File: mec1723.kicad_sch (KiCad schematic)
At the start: 19 parts, among them SW3001 SW_B3U-1000P_SMD, U3001 MEC1723N-B0-I/SZ, Y3001 Resonator_32.768kHz_ECX-31B

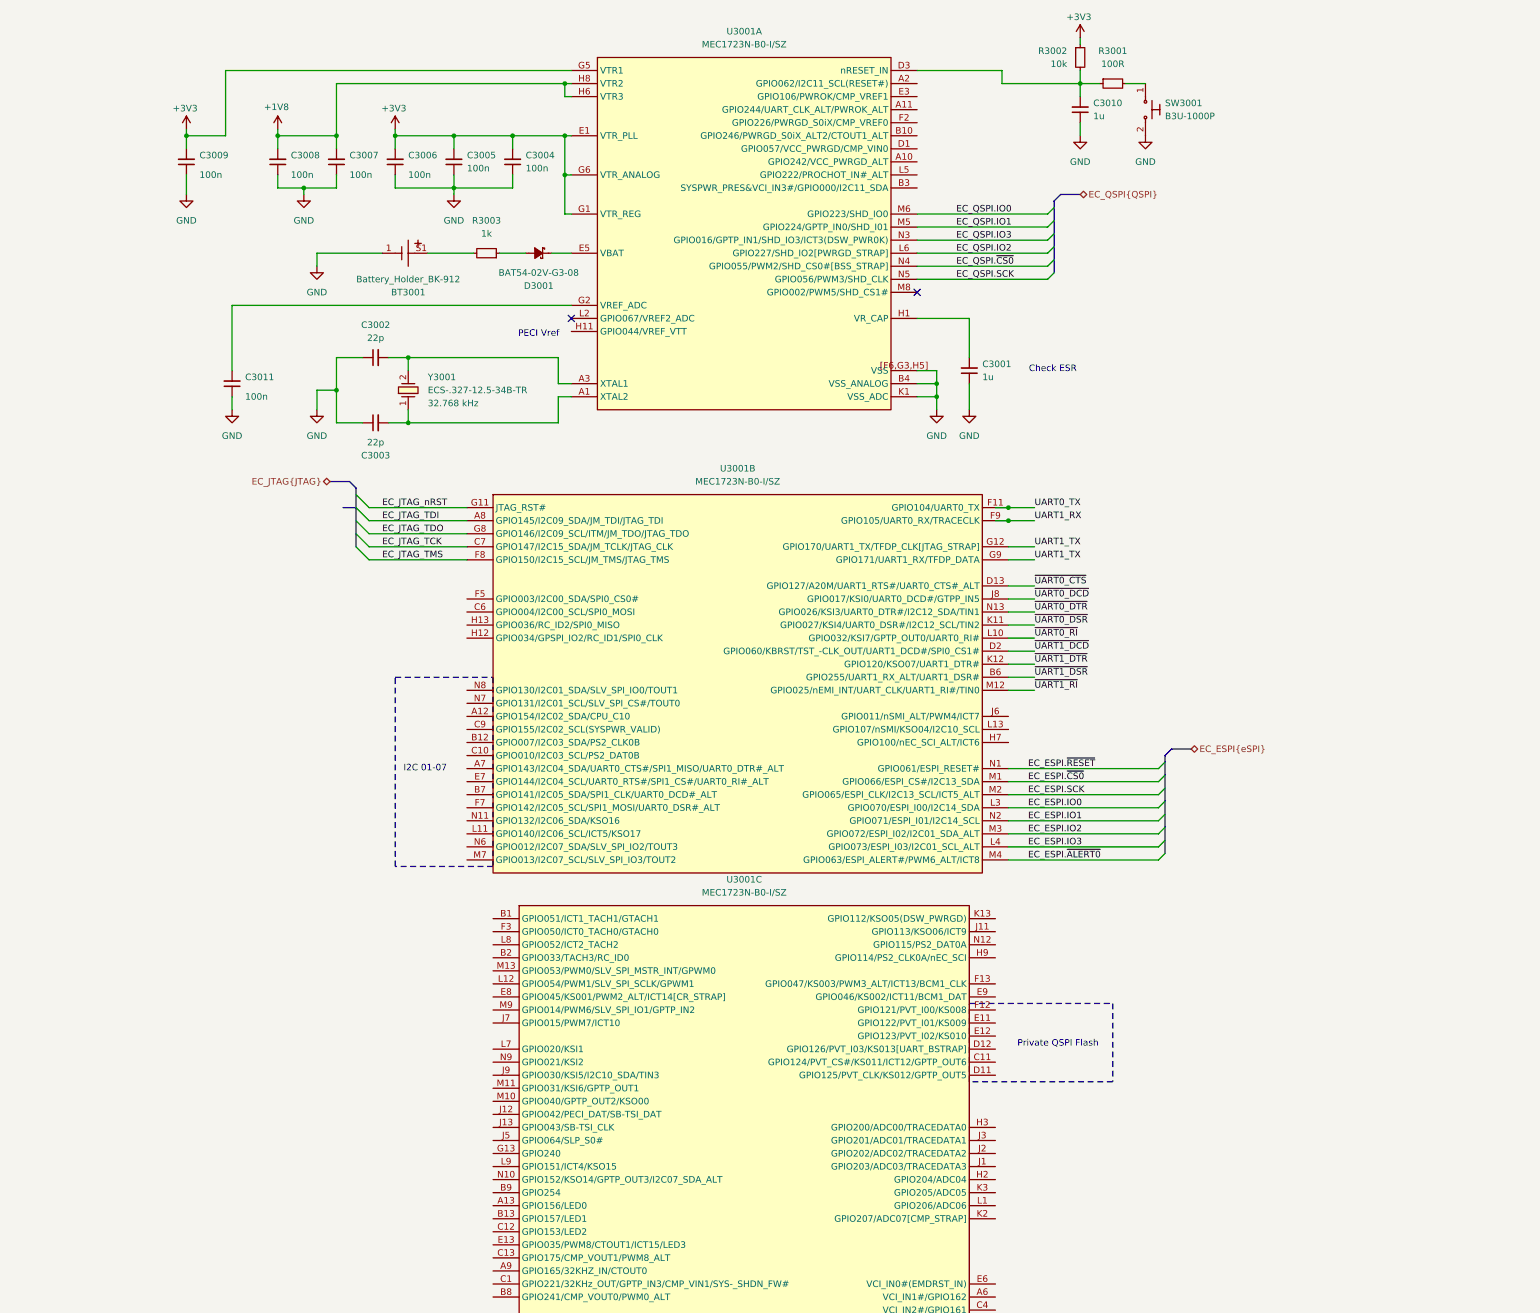
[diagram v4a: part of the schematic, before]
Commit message: [#103224] Change buffer ICs, change JTAG connector, move BSS_STRAP resistors to MEC1723 sheet
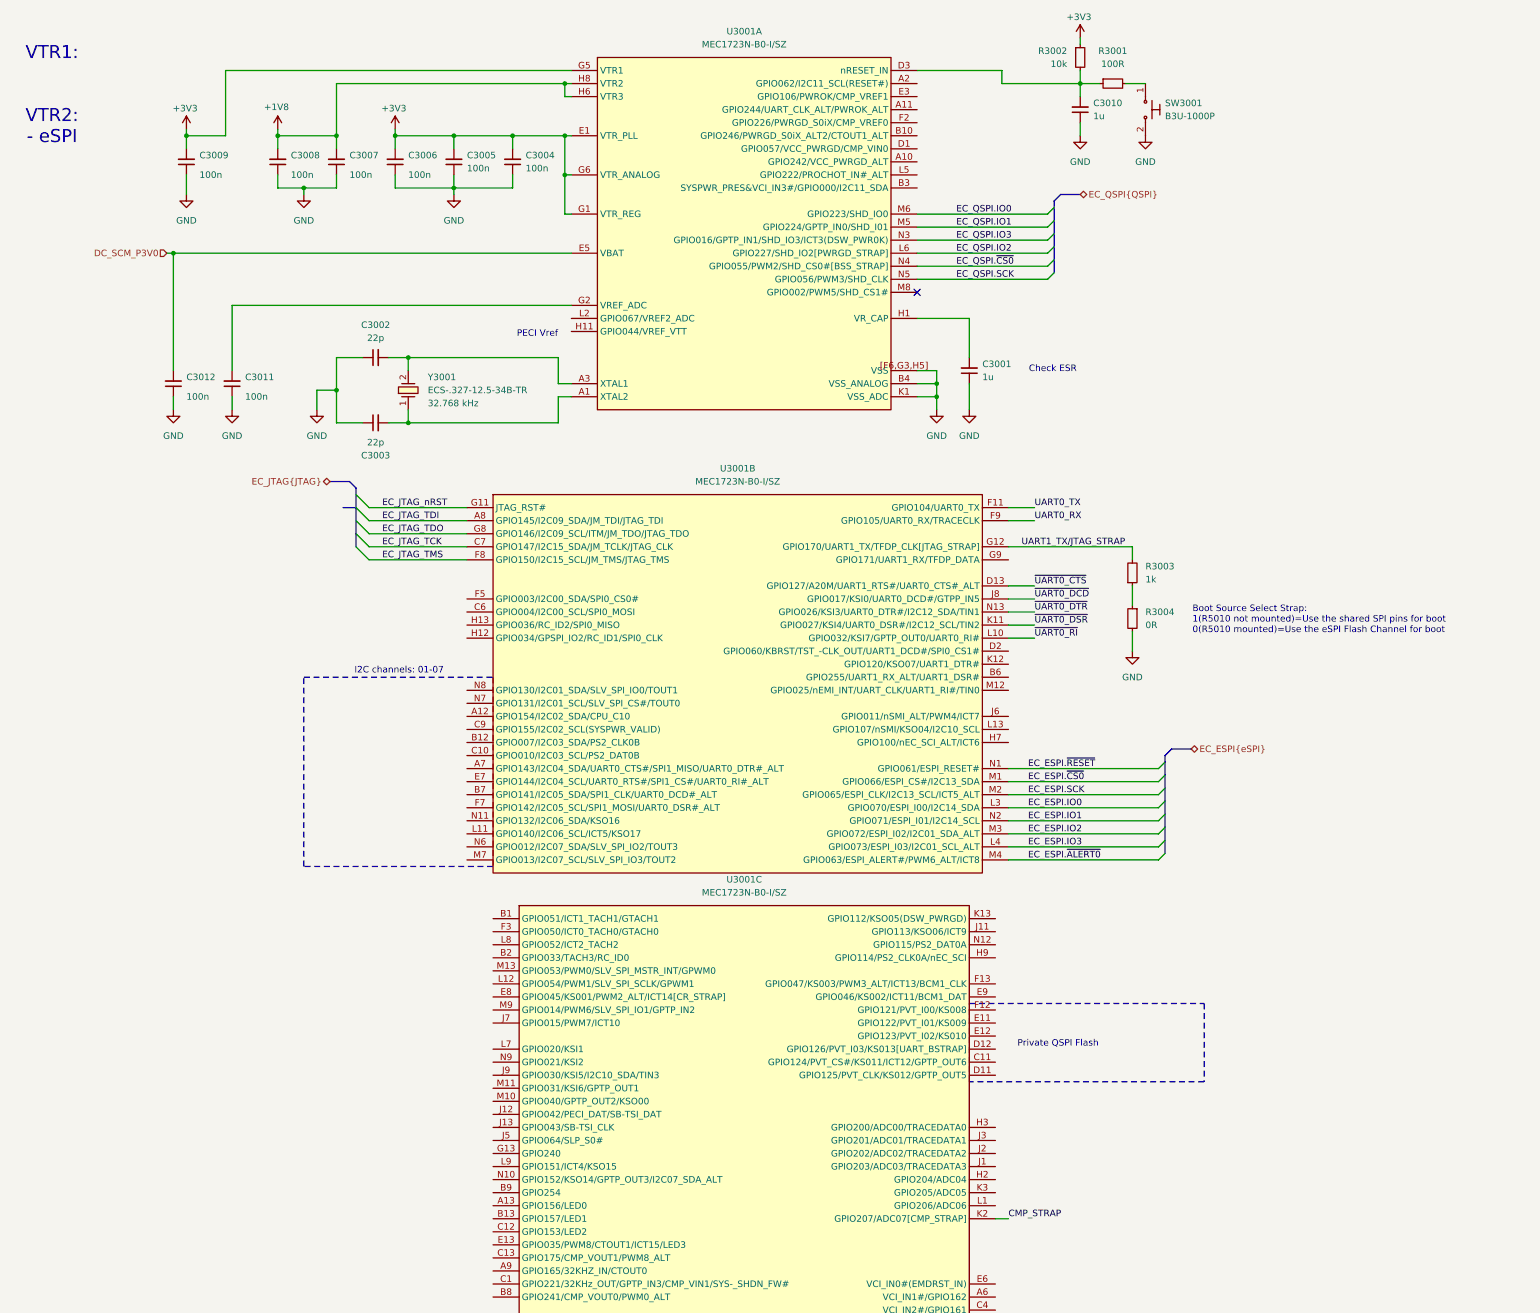
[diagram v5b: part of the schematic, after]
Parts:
- removed BT3001: Battery_Holder_BK-912, antmicro-footprints:Battery_Holder_BK-912, symbol Antmicro Symbols:Battery_Holder_BK-912
- removed D3001: BAT54-02V-G3-08, antmicro-footprints:SOD-523, symbol Antmicro Symbols:BAT54-02V-G3-08
- added C3012: C_100n_0402, antmicro-footprints:C_0402_1005Metric, symbol Capacitors0402:C_100n_0402
- added R3004: R_0R_0402, antmicro-footprints:R_0402_1005Metric, symbol Resistors0402:R_0R_0402
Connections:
- net GND: now also C3012.1, R3004.2
- net DC_SCM_P3V0: now reaches U3001.E5 (VBAT)
- net DC_SCM_P3V0: now also C3012.2
- net at R3003.1: now also R3004.1
- net UART1_TX/JTAG_STRAP: now reaches R3003.2
- net UART1_TX/JTAG_STRAP: now also U3001.G12 (GPIO170/UART1_TX/TFDP_CLK[JTAG_STRAP])
- net CMP_STRAP: now reaches U3001.K2 (GPIO207/ADC07[CMP_STRAP])
- net UART1_RX renamed UART0_RX
- net UART1_TX: no longer names the net of U3001.G9 (GPIO171/UART1_RX/TFDP_DATA)
- net UART1_TX: no longer U3001.G12 (GPIO170/UART1_TX/TFDP_CLK[JTAG_STRAP])
- net ~{UART1_DCD}: no longer names the net of U3001.D2 (GPIO060/KBRST/TST_-CLK_OUT/UART1_DCD#/SPI0_CS1#)
- net ~{UART1_DSR}: no longer names the net of U3001.B6 (GPIO255/UART1_RX_ALT/UART1_DSR#)
- net ~{UART1_DTR}: no longer names the net of U3001.K12 (GPIO120/KSO07/UART1_DTR#)
- net ~{UART1_RI}: no longer names the net of U3001.M12 (GPIO025/nEMI_INT/UART_CLK/UART1_RI#/TIN0)
- no-connect marks 2 -> 1
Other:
- note added: "Boot Source Select Strap: 1(R5010 not mounted)=Use the shared SPI pins for boot 0(R5010 mounted)=Use the eSPI Flash Channel for boot"
- note added: "I2C channels: 01-07"
- note added: "VTR1: VTR2: - eSPI"
- note removed: "I2C 01-07"

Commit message: [#103224] Add root schematic connections, add EMDRST button, add 1u decoupling capacitors, connect UART, add fiducials
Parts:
- removed R3001: R_100R_0402, antmicro-footprints:R_0402_1005Metric, symbol Antmicro Symbols:R_100R_0402
- removed R3002: R_10k_0402, antmicro-footprints:R_0402_1005Metric, symbol Antmicro Symbols:R_10k_0402
- added C3013: C_1u_6.3V_X6S_0402, antmicro-footprints:C_0402_1005Metric, symbol Antmicro Symbols:C_1u_6.3V_X6S_0402
- added C3014, C3015, C3016, C3017: C_1u_10V_X7R_0603, antmicro-footprints:C_0603_1608Metric, symbol Antmicro Symbols:C_1u_10V_X7R_0603
- added R3001, R3005: R_10k_0402, antmicro-footprints:R_0402_1005Metric, symbol Antmicro Symbols:R_10k_0402
- added R3002, R3006: R_100R_0402, antmicro-footprints:R_0402_1005Metric, symbol Antmicro Symbols:R_100R_0402
- added SW3002: SW_B3U-1000P_SMD, antmicro-footprints:SW_B3U-1000P_SMD, symbol Antmicro Symbols:SW_B3U-1000P_SMD
- R3004: now not fitted
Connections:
- net +1V8: now also C3015.2
- net +3V3: now also C3011.2, U3001.G2 (VREF_ADC), C3014.2, C3016.2, R3001.1, R3005.1
- net DC_SCM_P3V0: now also C3017.2
- net EC_QSPI.~{CS0}: now also R3003.2
- net GND: now also C3013.1, C3014.1, C3015.1, C3016.1, C3017.1, SW3002.2
- net at SW3001.1: now also R3002.2
- net nRESET_IN: now reaches C3010.2, U3001.D3 (nRESET_IN)
- net nRESET_IN: now also R3001.2, R3002.1
- net UART_BSTRAP: now reaches U3001.D12 (GPIO126/PVT_I03/KS013[UART_BSTRAP])
- net ~{VCI_IN0(EMDRST_IN)}: now reaches U3001.E6 (VCI_IN0#(EMDRST_IN))
- net ~{VCI_IN0(EMDRST_IN)}: now also C3013.2, R3005.2, R3006.1
- net CR_STRAP: now reaches U3001.E8 (GPIO045/KS001/PWM2_ALT/ICT14[CR_STRAP])
- net UART0_RX renamed EC_UART.RX
- net UART0_TX renamed EC_UART.TX
- net UART1_TX/JTAG_STRAP renamed JTAG_STRAP
- net JTAG_STRAP: no longer R3003.2
- new net: R3006.2, SW3002.1
- no-connect marks 1 -> 3
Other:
- note added: "ADC pins"
- note added: "BUTTONS"
- note added: "C3001 max. ESR = 100ohm"
- note added: "Connect GPIO after connecting all other, most important signals"
- note removed: "Check ESR"
- moved on the sheet: C3001, C3007, C3008, C3009

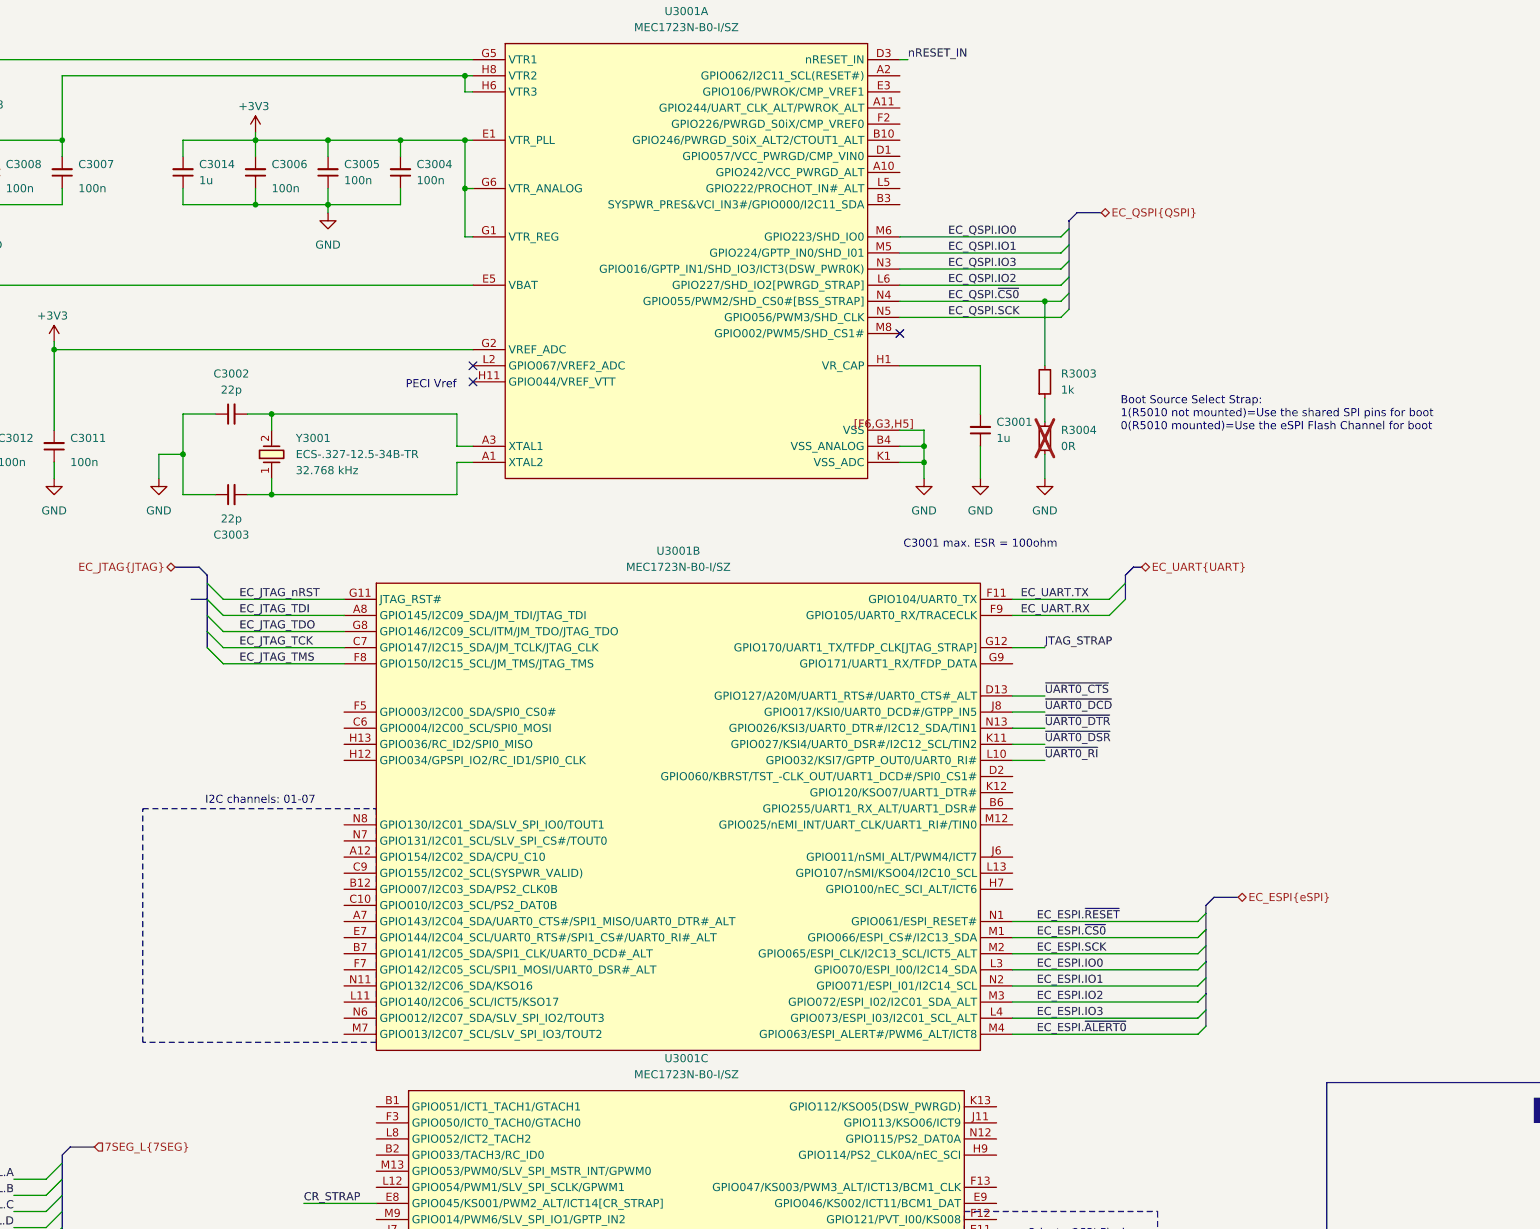
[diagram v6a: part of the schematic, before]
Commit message: [#103436] Start adding strap and configuration pins needed for power up
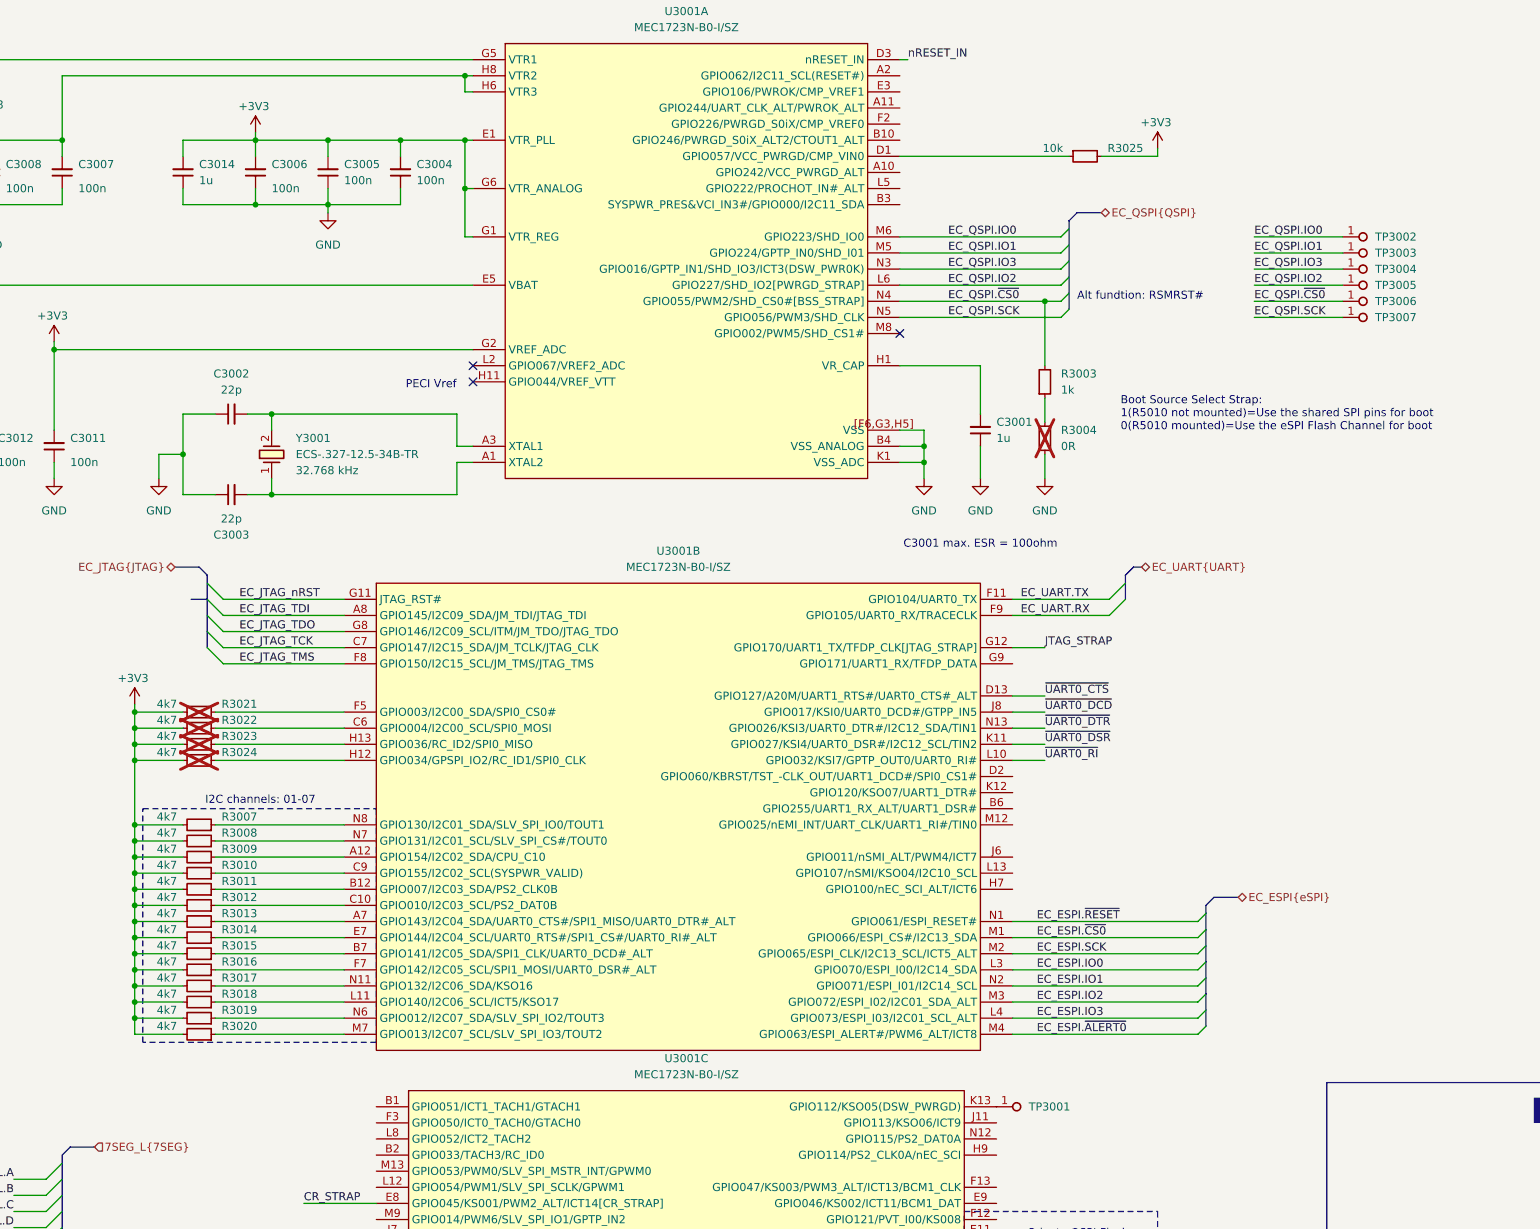
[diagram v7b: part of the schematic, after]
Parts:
- added R3007, R3008, R3009, R3010, R3011, R3012, R3013, R3014, R3015, R3016, R3017, R3018, R3019, R3020, R3021, R3022, R3023, R3024: R_4k7_0402, antmicro-footprints:R_0402_1005Metric, symbol antmicroResistors0402:R_4k7_0402
- added R3025: R_10k_0402, antmicro-footprints:R_0402_1005Metric, symbol antmicroResistors0402:R_10k_0402
- added TP3001, TP3002, TP3003, TP3004, TP3005, TP3006, TP3007: TP_1mm_SMD, antmicro-footprints:TP_SMD_1mm, symbol antmicroTestPoints:TP_1mm_SMD
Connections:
- net +3V3: now also R3007.2, R3008.2, R3009.2, R3010.2, R3011.2, R3012.2, R3013.2, R3014.2, R3015.2, R3016.2, R3017.2, R3018.2, R3019.2, R3020.2, R3021.2, R3022.2, R3023.2, R3024.2, R3025.2
- net EC_QSPI.IO0: now also TP3002.1
- net EC_QSPI.IO1: now also TP3003.1
- net EC_QSPI.IO2: now also TP3005.1
- net EC_QSPI.IO3: now also TP3004.1
- net EC_QSPI.SCK: now also TP3007.1
- net EC_QSPI.~{CS0}: now also TP3006.1
- net at U3001.D1 (GPIO057/VCC_PWRGD/CMP_VIN0): now also R3025.1
- net at U3001.K13 (GPIO112/KSO05(DSW_PWRGD)): now also TP3001.1
- net at U3001.A12 (GPIO154/I2C02_SDA/CPU_C10): now also R3009.1
- net at U3001.A7 (GPIO143/I2C04_SDA/UART0_CTS#/SPI1_MISO/UART0_DTR#_ALT): now also R3013.1
- net at U3001.B12 (GPIO007/I2C03_SDA/PS2_CLK0B): now also R3011.1
- net at U3001.B7 (GPIO141/I2C05_SDA/SPI1_CLK/UART0_DCD#_ALT): now also R3015.1
- net at U3001.C10 (GPIO010/I2C03_SCL/PS2_DAT0B): now also R3012.1
- net at U3001.C6 (GPIO004/I2C00_SCL/SPI0_MOSI): now also R3022.1
- net at U3001.C9 (GPIO155/I2C02_SCL(SYSPWR_VALID)): now also R3010.1
- net at U3001.E7 (GPIO144/I2C04_SCL/UART0_RTS#/SPI1_CS#/UART0_RI#_ALT): now also R3014.1
- net at U3001.F5 (GPIO003/I2C00_SDA/SPI0_CS0#): now also R3021.1
- net at U3001.F7 (GPIO142/I2C05_SCL/SPI1_MOSI/UART0_DSR#_ALT): now also R3016.1
- net at U3001.H12 (GPIO034/GPSPI_IO2/RC_ID1/SPI0_CLK): now also R3024.1
- net at U3001.H13 (GPIO036/RC_ID2/SPI0_MISO): now also R3023.1
- net at U3001.L11 (GPIO140/I2C06_SCL/ICT5/KSO17): now also R3018.1
- net at U3001.M7 (GPIO013/I2C07_SCL/SLV_SPI_IO3/TOUT2): now also R3020.1
- net at U3001.N11 (GPIO132/I2C06_SDA/KSO16): now also R3017.1
- net at U3001.N6 (GPIO012/I2C07_SDA/SLV_SPI_IO2/TOUT3): now also R3019.1
- net at U3001.N7 (GPIO131/I2C01_SCL/SLV_SPI_CS#/TOUT0): now also R3008.1
- net at U3001.N8 (GPIO130/I2C01_SDA/SLV_SPI_IO0/TOUT1): now also R3007.1
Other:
- note added: "Alt fundtion: RSMRST#"
